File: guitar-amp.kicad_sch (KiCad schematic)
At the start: 55 parts, among them J1 Speaker Output, J2 Input, J3 AC Mains, T1 5W OT, T2 Transformer_1P_2S

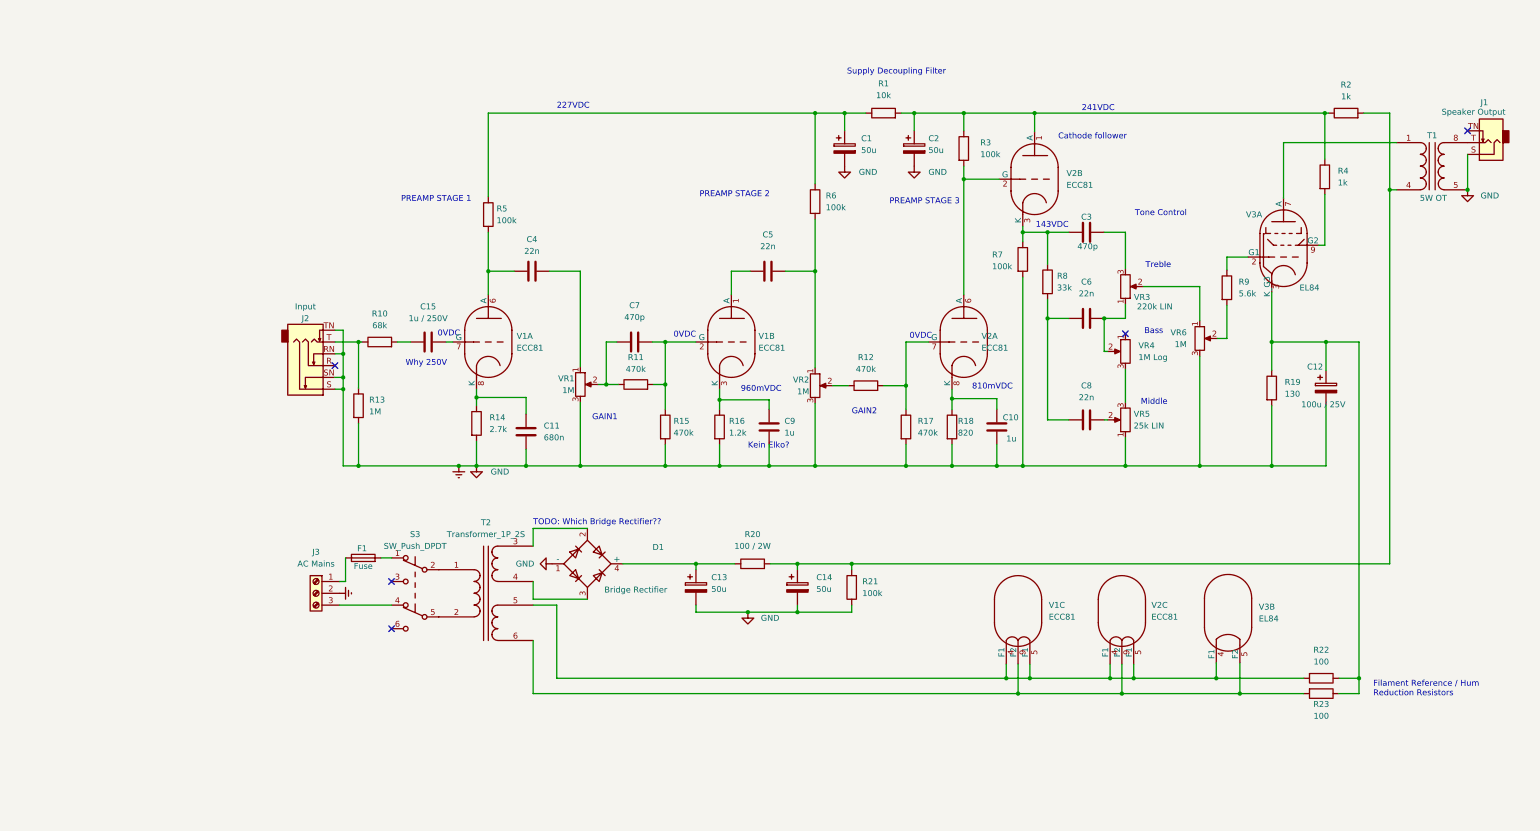
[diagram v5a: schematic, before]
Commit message: Roughly layout the components on the PCB
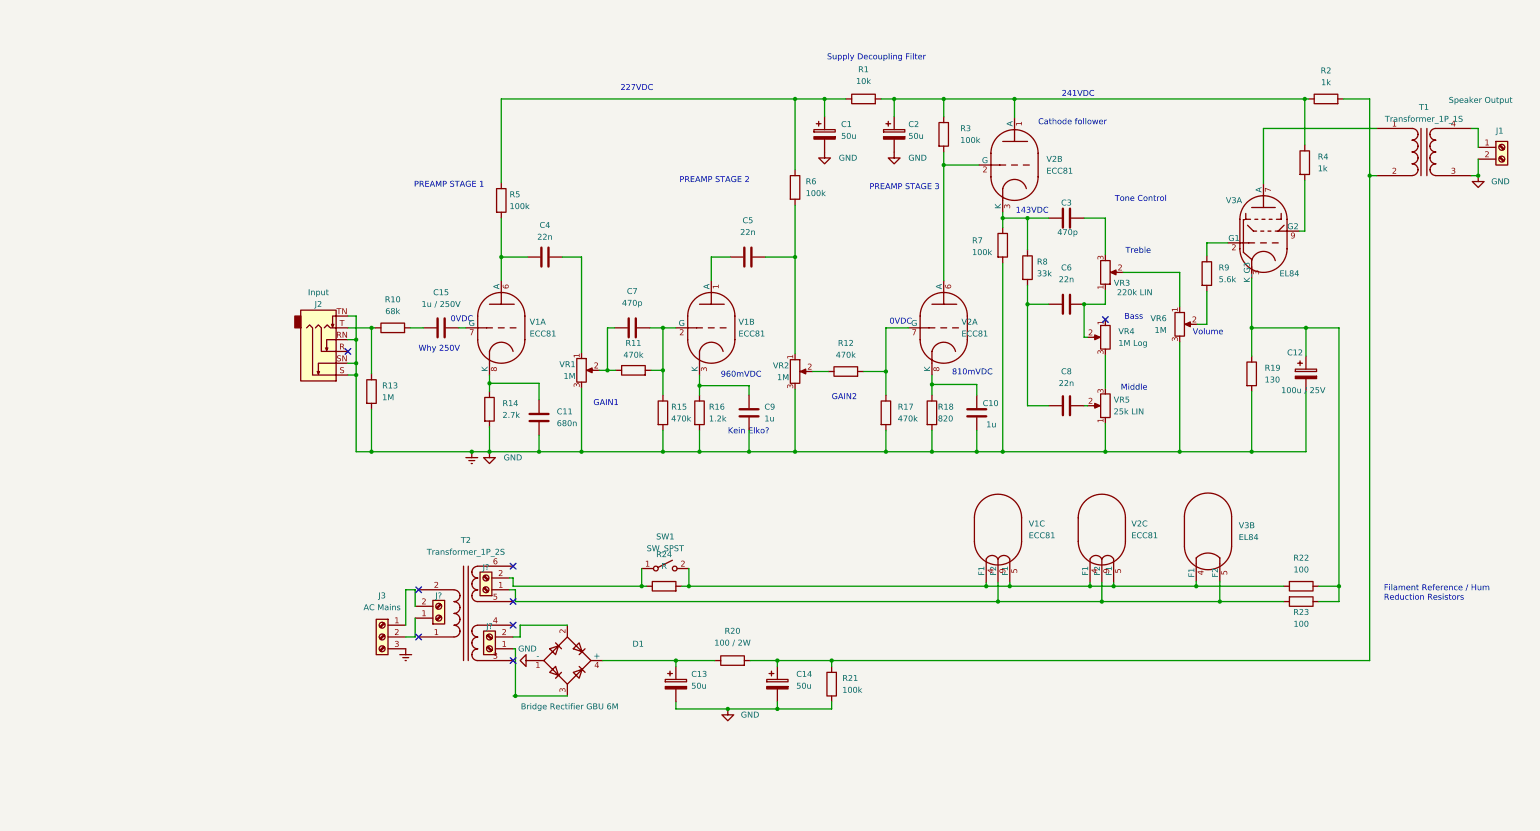
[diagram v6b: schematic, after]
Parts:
- removed F1: Fuse, Fuse:Fuseholder_Cylinder-5x20mm_Schurter_0031_8201_Horizontal_Open, symbol Device:Fuse
- removed J1: Speaker Output, TerminalBlock_Phoenix:TerminalBlock_Phoenix_MKDS-1,5-2-5.08_1x02_P5.08mm_Horizontal, symbol Connector:AudioJack2_SwitchT
- removed S3: SW_Push_DPDT, Button_Switch_THT:SW_CuK_JS202011CQN_DPDT_Straight, symbol Switch:SW_Push_DPDT
- removed T1: 5W OT, symbol Device:Transformer_1P_1S_SO8
- added J1: Speaker Output, TerminalBlock_RND:TerminalBlock_RND_205-00001_1x02_P5.00mm_Horizontal, symbol Connector:Screw_Terminal_01x02
- added J? (x3): Screw_Terminal_01x02, symbol Connector:Screw_Terminal_01x02
- added R24: R, Resistor_THT:R_Axial_Power_L20.0mm_W6.4mm_P25.40mm, symbol Device:R
- added SW1: SW_SPST, Button_Switch_THT:SW_CuK_JS202011CQN_DPDT_Straight, symbol Switch:SW_SPST
- added T1: Transformer_1P_1S, TerminalBlock_RND:TerminalBlock_RND_205-00003_1x04_P5.00mm_Horizontal, symbol Device:Transformer_1P_1S
- D1: value Bridge Rectifier -> Bridge Rectifier GBU 6M; footprint Diode_THT:Diode_Bridge_32.0x5.6x17.0mm_P10.0mm_P7.5mm -> Diode_THT:Diode_Bridge_Vishay_GBU
- J3: footprint (none) -> TerminalBlock_RND:TerminalBlock_RND_205-00002_1x03_P5.00mm_Horizontal
- V1, V2, V3: footprint Valve:Valve_Noval_P -> Valve:Valve_ECC-83-1
- VR1, VR2, VR6: footprint Potentiometer_THT:Potentiometer_Piher_PT-15-V15_Vertical -> Potentiometer_THT:Potentiometer_Alps_RK163_Single_Horizontal
- VR3: Function (none) -> Treble
- VR4: footprint Potentiometer_THT:Potentiometer_Piher_PT-15-V15_Vertical -> Potentiometer_THT:Potentiometer_Alps_RK163_Single_Horizontal; Function (none) -> Bass
- VR5: Function (none) -> Middle
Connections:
- net Earth: now also J3.3 (Pin_3), J1.2 (Pin_2), T1.3 (SA); no longer J3.2 (Pin_2)
- net at D1.2: now also J?.2 (Pin_2); no longer T2.3 (SA)
- net at D1.3: now also J?.1 (Pin_1); no longer T2.4 (SB)
- net at C14.1, R2.2, R20.2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: now also T1.2 (AB)
- net at J3.1 (Pin_1): now also J?.2 (Pin_2)
- net at R22.2, V1.4 (F1), V1.5 (F1)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: now also R24.2, SW1.2 (B); no longer T2.5 (SC)
- net at R23.2, V1.9 (F2), V2.9 (F2)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: now also J?.1 (Pin_1); no longer T2.6 (SD)
- net at V3.7 (A): now also T1.1 (AA)
- new net: J?.2 (Pin_2), R24.1, SW1.1 (A)
- new net: J3.2 (Pin_2), J?.1 (Pin_1)
- new net: J1.1 (Pin_1), T1.4 (SB)
- no-connect marks 5 -> 8
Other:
- note added: "Volume"
- note removed: "TODO: Which Bridge Rectifier??"
- company: (none) -> Besmer Labs
- title: (none) -> Guitar Amp based on High Octane
- moved on the sheet: C1, C10, C11, C12, C13, C14, C15, C2, C3, C4, C5, C6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

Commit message: First draft of routing
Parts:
- J4, J5, J6: renamed from J?; footprint (none) -> TerminalBlock_RND:TerminalBlock_RND_205-00001_1x02_P5.00mm_Horizontal
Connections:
- net HighDC_Trafo2: now reaches D1.3, J6.1 (Pin_1)
- net HighDC_Trafo1: now reaches D1.2, J6.2 (Pin_2)
- net HighDC_V1B_Anode: now reaches C5.1, V1.1 (A)
- net HighDC_Prefilter: now reaches C13.1, D1.4 (+), R20.1
- net HighDC_241VDC: now reaches C2.1, R1.2, R2.1, R3.1, R4.1, V2.1 (A)
- net HighDC_Post: now reaches C14.1, R2.2, R20.2, R21.2, T1.2 (AB)
- net AC_N: now reaches J3.2 (Pin_2), J4.1 (Pin_1)
- net AC_L: now reaches J3.1 (Pin_1), J4.2 (Pin_2)
- net HighDC_143VDC: now reaches C3.1, R7.1, R8.1, V2.3 (K)
- net HighDC_V2A_Anode: now reaches R3.2, V2.2 (G), V2.6 (A)
- net HighDC_OT: now reaches T1.1 (AA), V3.7 (A)
- net HighDC_227VDC: now reaches C1.1, R1.1, R5.1, R6.1
- net HighDC_GateValve3: now reaches R4.2, V3.9 (G2)
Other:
- note removed: "143VDC"
- note removed: "227VDC"
- note removed: "241VDC"
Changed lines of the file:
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@@
   (junction (at 157.48 34.544) (diameter 0) (color 0 0 0 0)
-  )
-  (junction (at 65.278 163.068) (diameter 0) (color 0 0 0 0)
   )
   (junction (at 121.666 165.862) (diameter 0) (color 0 0 0 0)
@@
   (no_connect (at 29.21 88.9))
   (no_connect (at 64.77 135.128))
+  (no_connect (at 44.45 150.368))
   (no_connect (at 44.45 140.208))
-  (no_connect (at 44.45 150.368))
   (no_connect (at 64.77 147.828))
+  (no_connect (at 64.77 142.748))
   (no_connect (at 64.77 155.448))
-  (no_connect (at 64.77 142.748))
   (no_connect (at 192.278 82.042))
   (wire (pts (xy 99.822 155.448) (xy 99.822 156.718))
@@
     (stroke (width 0) (type default) (color 0 0 0 0))
   )
-  (wire (pts (xy 64.77 163.068) (xy 65.278 163.068))
-    (stroke (width 0) (type default) (color 0 0 0 0))
-  )
   (wire (pts (xy 107.442 68.58) (xy 111.506 68.58))
     (stroke (width 0) (type default) (color 0 0 0 0))
@@
   )
   (text "960mVDC\n" (at 109.474 94.742 0)
-    (effects (font (size 1.27 1.27)) (justify left bottom))
-  )
-  (text "227VDC" (at 87.884 33.02 0)
     (effects (font (size 1.27 1.27)) (justify left bottom))
   )
@@
     (effects (font (size 1.27 1.27)) (justify right bottom))
   )
-  (text "241VDC" (at 182.88 34.29 0)
-    (effects (font (size 1.27 1.27)) (justify left bottom))
-  )
   (text "PREAMP STAGE 1" (at 43.434 53.848 0)
     (effects (font (size 1.27 1.27)) (justify left bottom))
@@
     (effects (font (size 1.27 1.27)) (justify left bottom))
   )
-  (text "143VDC" (at 172.974 59.436 0)
-    (effects (font (size 1.27 1.27)) (justify left bottom))
-  )
   (text "810mVDC\n" (at 159.258 94.234 0)
     (effects (font (size 1.27 1.27)) (justify left bottom))
@@
   )
   (text "Tone Control" (at 194.31 56.896 0)
+    (effects (font (size 1.27 1.27)) (justify left bottom))
+  )
+  (label "HighDC_227VDC" (at 66.802 34.544 0)
+    (effects (font (size 1.27 1.27)) (justify left bottom))
+  )
+  (label "HighDC_Trafo2" (at 65.278 163.068 0)
+    (effects (font (size 1.27 1.27)) (justify left bottom))
+  )
+  (label "HighDC_241VDC" (at 183.134 34.544 0)
+    (effects (font (size 1.27 1.27)) (justify left bottom))
+  )
+  (label "HighDC_OT" (at 226.568 40.894 0)
+    (effects (font (size 1.27 1.27)) (justify left bottom))
+  )
+  (label "HighDC_Trafo1" (at 66.548 147.828 0)
+    (effects (font (size 1.27 1.27)) (justify left bottom))
+  )
+  (label "HighDC_V1B_Anode" (at 107.442 73.66 90)
+    (effects (font (size 1.27 1.27)) (justify left bottom))
+  )
+  (label "AC_N" (at 43.688 146.304 270)
+    (effects (font (size 1.27 1.27)) (justify right bottom))
+  )
+  (label "HighDC_Post" (at 136.144 155.448 0)
+    (effects (font (size 1.27 1.27)) (justify left bottom))
+  )
+  (label "AC_L" (at 41.656 140.208 90)
+    (effects (font (size 1.27 1.27)) (justify left bottom))
+  )
+  (label "HighDC_Prefilter" (at 88.392 155.448 0)
+    (effects (font (size 1.27 1.27)) (justify left bottom))
+  )
+  (label "HighDC_V2A_Anode" (at 157.48 55.118 270)
+    (effects (font (size 1.27 1.27)) (justify right bottom))
+  )
+  (label "HighDC_GateValve3" (at 235.204 62.992 0)
+    (effects (font (size 1.27 1.27)) (justify left bottom))
+  )
+  (label "HighDC_143VDC" (at 170.18 60.198 0)
     (effects (font (size 1.27 1.27)) (justify left bottom))
   )
   (symbol (lib_id "Connector:Screw_Terminal_01x02") (at 59.69 152.908 180) (unit 1)
     (in_bom yes) (on_board yes)
-    (property "Reference" "J?" (id 0) (at 59.69 148.082 0))
+    (property "Reference" "J6" (id 0) (at 59.69 148.082 0))
     (property "Value" "Screw_Terminal_01x02" (id 1) (at 59.69 146.304 0)
       (effects (font (size 1.27 1.27)) hide)
     )
-    (property "Footprint" "" (id 2) (at 59.69 152.908 0)
+    (property "Footprint" "TerminalBlock_RND:TerminalBlock_RND_205-00001_1x02_P5.00mm_Horizontal" (id 2) (at 59.69 152.908 0)
       (effects (font (size 1.27 1.27)) hide)
     )
@@
   (symbol (lib_id "Connector:Screw_Terminal_01x02") (at 48.768 146.304 0) (mirror x) (unit 1)
     (in_bom yes) (on_board yes)
-    (property "Reference" "J?" (id 0) (at 48.768 141.478 0))
+    (property "Reference" "J4" (id 0) (at 48.768 141.478 0))
     (property "Value" "Screw_Terminal_01x02" (id 1) (at 48.768 139.7 0)
       (effects (font (size 1.27 1.27)) hide)
     )
-    (property "Footprint" "" (id 2) (at 48.768 146.304 0)
+    (property "Footprint" "TerminalBlock_RND:TerminalBlock_RND_205-00001_1x02_P5.00mm_Horizontal" (id 2) (at 48.768 146.304 0)
       (effects (font (size 1.27 1.27)) hide)
     )
@@
   (symbol (lib_id "Connector:Screw_Terminal_01x02") (at 58.928 140.208 180) (unit 1)
     (in_bom yes) (on_board yes)
-    (property "Reference" "J?" (id 0) (at 58.928 135.382 0))
+    (property "Reference" "J5" (id 0) (at 58.928 135.382 0))
     (property "Value" "Screw_Terminal_01x02" (id 1) (at 58.928 133.604 0)
       (effects (font (size 1.27 1.27)) hide)
     )
-    (property "Footprint" "" (id 2) (at 58.928 140.208 0)
+    (property "Footprint" "TerminalBlock_RND:TerminalBlock_RND_205-00001_1x02_P5.00mm_Horizontal" (id 2) (at 58.928 140.208 0)
       (effects (font (size 1.27 1.27)) hide)
     )
@@
       (reference "J3") (unit 1) (value "AC Mains") (footprint "TerminalBlock_RND:TerminalBlock_RND_205-00002_1x03_P5.00mm_Horizontal")
     )
+    (path "/386c3d79-1615-4187-942d-eed7f8a31816"
+      (reference "J4") (unit 1) (value "Screw_Terminal_01x02") (footprint "TerminalBlock_RND:TerminalBlock_RND_205-00001_1x02_P5.00mm_Horizontal")
+    )
+    (path "/81a22f5d-d2b7-4d0c-af28-7098557ce51b"
+      (reference "J5") (unit 1) (value "Screw_Terminal_01x02") (footprint "TerminalBlock_RND:TerminalBlock_RND_205-00001_1x02_P5.00mm_Horizontal")
+    )
     (path "/02e4fc72-e2c9-4f9e-8ff9-18ab383b01b7"
-      (reference "J?") (unit 1) (value "Screw_Terminal_01x02") (footprint "")
-    )
-    (path "/386c3d79-1615-4187-942d-eed7f8a31816"
-      (reference "J?") (unit 1) (value "Screw_Terminal_01x02") (footprint "")
-    )
-    (path "/81a22f5d-d2b7-4d0c-af28-7098557ce51b"
-      (reference "J?") (unit 1) (value "Screw_Terminal_01x02") (footprint "")
+      (reference "J6") (unit 1) (value "Screw_Terminal_01x02") (footprint "TerminalBlock_RND:TerminalBlock_RND_205-00001_1x02_P5.00mm_Horizontal")
     )
     (path "/eb0eca1a-a845-4c07-9c98-8a80d6f813f5"

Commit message: Routing improvements
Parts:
- added H1, H2, H3, H4: MountingHole, MountingHole:MountingHole_3.2mm_M3, symbol Mechanical:MountingHole
- C12: footprint Capacitor_THT:CP_Radial_D6.3mm_P2.50mm -> Capacitor_THT:CP_Radial_D8.0mm_P3.80mm
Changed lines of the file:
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@@
     (pin "2")
+  )
+  (symbol (lib_id "Mechanical:MountingHole") (at 153.162 187.452 0) (unit 1)
+    (in_bom yes) (on_board yes) (fields_autoplaced)
+    (property "Reference" "H4" (id 0) (at 156.718 186.1819 0)
+      (effects (font (size 1.27 1.27)) (justify left))
+    )
+    (property "Value" "MountingHole" (id 1) (at 156.718 188.7219 0)
+      (effects (font (size 1.27 1.27)) (justify left))
+    )
+    (property "Footprint" "MountingHole:MountingHole_3.2mm_M3" (id 2) (at 153.162 187.452 0)
+      (effects (font (size 1.27 1.27)) hide)
+    )
+    (property "Datasheet" "~" (id 3) (at 153.162 187.452 0)
+      (effects (font (size 1.27 1.27)) hide)
+    )
   )
   (symbol (lib_id "Valve:ECC81") (at 107.442 83.82 0) (unit 2)
@@
     (pin "2")
   )
+  (symbol (lib_id "Mechanical:MountingHole") (at 94.742 187.452 0) (unit 1)
+    (in_bom yes) (on_board yes) (fields_autoplaced)
+    (property "Reference" "H1" (id 0) (at 98.298 186.1819 0)
+      (effects (font (size 1.27 1.27)) (justify left))
+    )
+    (property "Value" "MountingHole" (id 1) (at 98.298 188.7219 0)
+      (effects (font (size 1.27 1.27)) (justify left))
+    )
+    (property "Footprint" "MountingHole:MountingHole_3.2mm_M3" (id 2) (at 94.742 187.452 0)
+      (effects (font (size 1.27 1.27)) hide)
+    )
+    (property "Datasheet" "~" (id 3) (at 94.742 187.452 0)
+      (effects (font (size 1.27 1.27)) hide)
+    )
+  )
   (symbol (lib_id "Device:C_Polarized") (at 131.826 42.164 0) (unit 1)
     (in_bom yes) (on_board yes) (fields_autoplaced)
@@
     (pin "1")
   )
+  (symbol (lib_id "Mechanical:MountingHole") (at 133.604 187.452 0) (unit 1)
+    (in_bom yes) (on_board yes) (fields_autoplaced)
+    (property "Reference" "H3" (id 0) (at 137.16 186.1819 0)
+      (effects (font (size 1.27 1.27)) (justify left))
+    )
+    (property "Value" "MountingHole" (id 1) (at 137.16 188.7219 0)
+      (effects (font (size 1.27 1.27)) (justify left))
+    )
+    (property "Footprint" "MountingHole:MountingHole_3.2mm_M3" (id 2) (at 133.604 187.452 0)
+      (effects (font (size 1.27 1.27)) hide)
+    )
+    (property "Datasheet" "~" (id 3) (at 133.604 187.452 0)
+      (effects (font (size 1.27 1.27)) hide)
+    )
+  )
   (symbol (lib_id "Device:C_Polarized") (at 235.458 93.726 0) (unit 1)
     (in_bom yes) (on_board yes)
@@
       (effects (font (size 1.27 1.27)) (justify left))
     )
-    (property "Footprint" "Capacitor_THT:CP_Radial_D6.3mm_P2.50mm" (id 2) (at 236.4232 97.536 0)
+    (property "Footprint" "Capacitor_THT:CP_Radial_D8.0mm_P3.80mm" (id 2) (at 236.4232 97.536 0)
       (effects (font (size 1.27 1.27)) hide)
     )
@@
     (pin "9")
   )
+  (symbol (lib_id "Mechanical:MountingHole") (at 114.3 187.452 0) (unit 1)
+    (in_bom yes) (on_board yes) (fields_autoplaced)
+    (property "Reference" "H2" (id 0) (at 117.856 186.1819 0)
+      (effects (font (size 1.27 1.27)) (justify left))
+    )
+    (property "Value" "MountingHole" (id 1) (at 117.856 188.7219 0)
+      (effects (font (size 1.27 1.27)) (justify left))
+    )
+    (property "Footprint" "MountingHole:MountingHole_3.2mm_M3" (id 2) (at 114.3 187.452 0)
+      (effects (font (size 1.27 1.27)) hide)
+    )
+    (property "Datasheet" "~" (id 3) (at 114.3 187.452 0)
+      (effects (font (size 1.27 1.27)) hide)
+    )
+  )
   (symbol (lib_id "Device:C") (at 183.896 78.74 90) (unit 1)
     (in_bom yes) (on_board yes) (fields_autoplaced)
@@
     )
     (path "/d07d7514-b774-4322-8d62-e2d14f87d2ae"
-      (reference "C12") (unit 1) (value "100u / 25V") (footprint "Capacitor_THT:CP_Radial_D6.3mm_P2.50mm")
+      (reference "C12") (unit 1) (value "100u / 25V") (footprint "Capacitor_THT:CP_Radial_D8.0mm_P3.80mm")
     )
     (path "/b75fbf3a-5bd9-43fd-b230-2ee6aeb56be1"
@@
       (reference "D1") (unit 1) (value "Bridge Rectifier GBU 6M") (footprint "Diode_THT:Diode_Bridge_Vishay_GBU")
     )
+    (path "/a1b1c5c3-8cd9-41cd-8be9-d9848e2a9c67"
+      (reference "H1") (unit 1) (value "MountingHole") (footprint "MountingHole:MountingHole_3.2mm_M3")
+    )
+    (path "/e0e7593c-7213-4c9f-a2b6-f4e0393cff92"
+      (reference "H2") (unit 1) (value "MountingHole") (footprint "MountingHole:MountingHole_3.2mm_M3")
+    )
+    (path "/cc17858a-bca7-444a-a959-65f8f38e9b95"
+      (reference "H3") (unit 1) (value "MountingHole") (footprint "MountingHole:MountingHole_3.2mm_M3")
+    )
+    (path "/046b86e9-a11e-4971-955c-121188d06d8c"
+      (reference "H4") (unit 1) (value "MountingHole") (footprint "MountingHole:MountingHole_3.2mm_M3")
+    )
     (path "/f3ad5e14-e18f-4c98-bc77-e1d7d666db53"
